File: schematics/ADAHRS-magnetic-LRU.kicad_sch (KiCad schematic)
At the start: 40 parts, among them Q1 2N2222, Q2 IRF7171M, Q3 Q2 - 2N2907, Q4 2N2222, Q5 IRF7171M, U1 OPA365-EP, U3 OPA365-EP

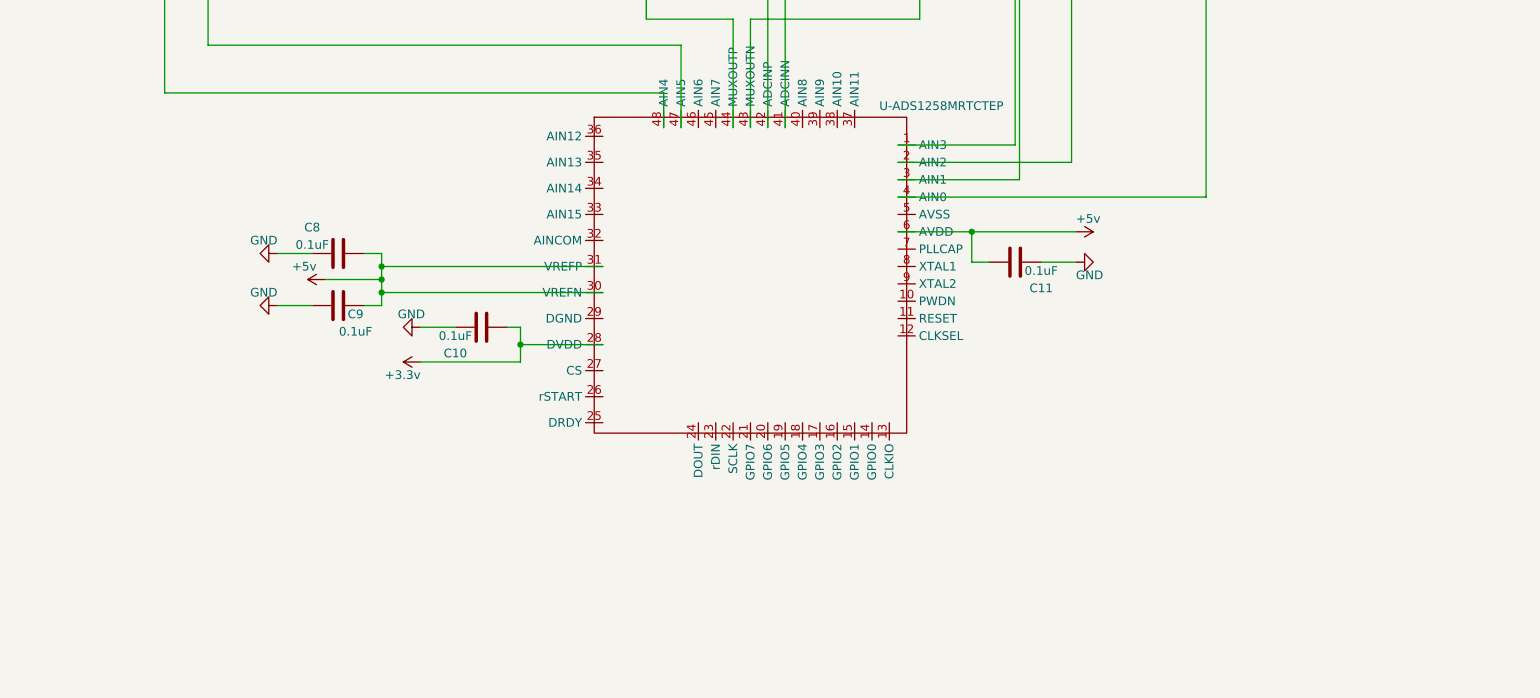
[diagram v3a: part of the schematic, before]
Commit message: Crystal oscillator and global var for MCU
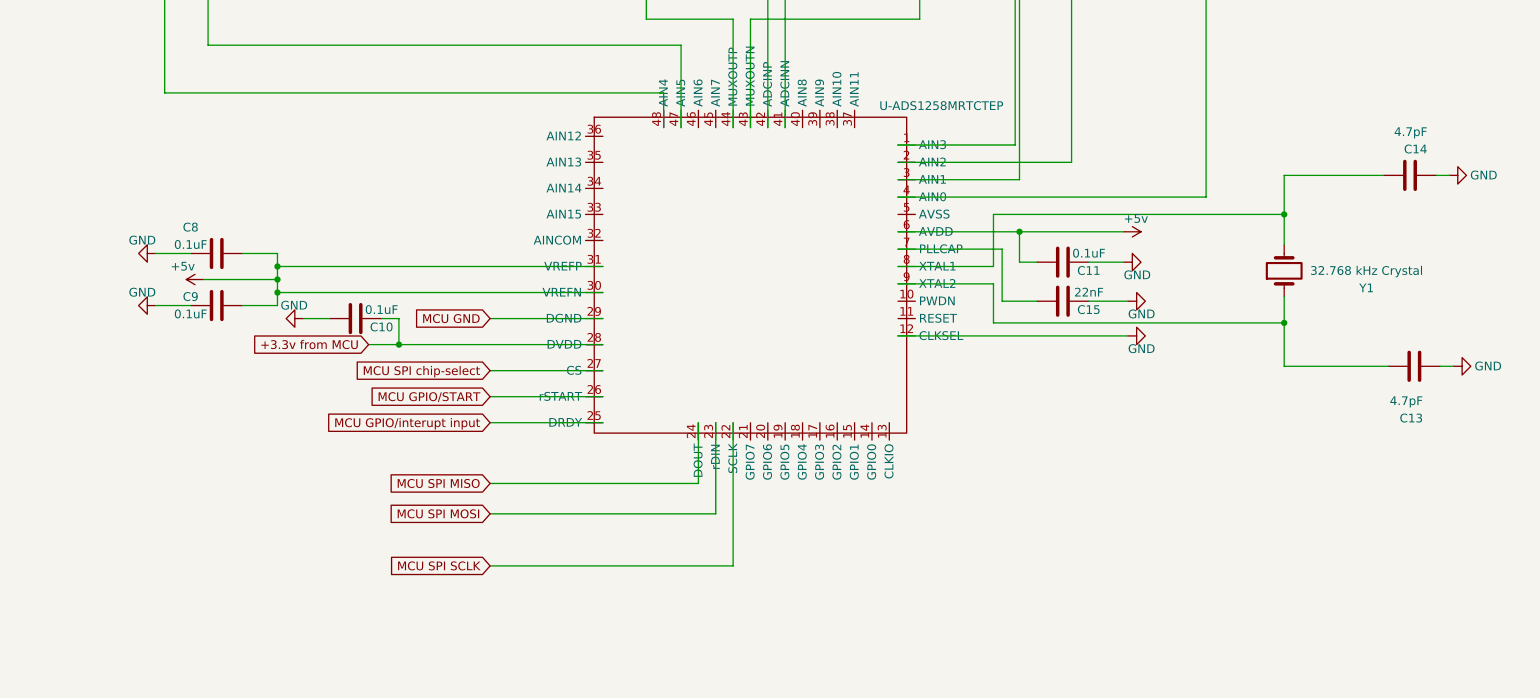
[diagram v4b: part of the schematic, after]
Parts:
- added C13, C14: 4.7pF, symbol Device:C
- added C15: 22nF, symbol Device:C
- added Y1: 32.768 kHz Crystal, symbol Device:Crystal
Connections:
- net +18v: now also U-ADS1258MRTCTEP.12 (CLKSEL), C13.1, C14.1, C15.1
- net MCU SPI SCLK: now reaches U-ADS1258MRTCTEP.22 (SCLK)
- net MCU SPI MOSI: now reaches U-ADS1258MRTCTEP.23 (rDIN)
- net MCU SPI MISO: now reaches U-ADS1258MRTCTEP.24 (DOUT)
- net MCU GPIO/interupt input: now reaches U-ADS1258MRTCTEP.25 (DRDY)
- net MCU GPIO/START: now reaches U-ADS1258MRTCTEP.26 (rSTART)
- net MCU SPI chip-select: now reaches U-ADS1258MRTCTEP.27 (CS)
- net MCU GND: now reaches U-ADS1258MRTCTEP.29 (DGND)
- net at U-ADS1258MRTCTEP.7 (PLLCAP): now also C15.2
- net at U-ADS1258MRTCTEP.8 (XTAL1): now also C14.2, Y1.2
- net at U-ADS1258MRTCTEP.9 (XTAL2): now also C13.2, Y1.1
- net +3.3v renamed +3.3v from MCU
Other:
- moved on the sheet: C10, C11, C8, C9

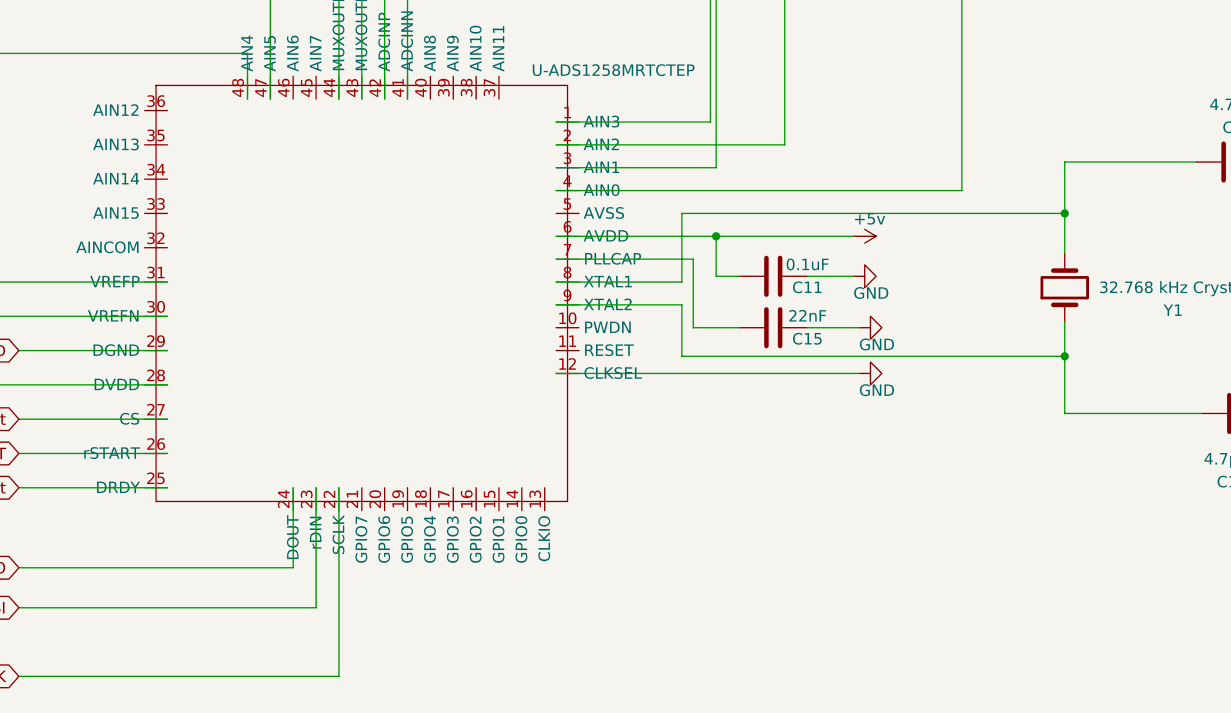
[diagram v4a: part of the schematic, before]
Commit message: revised capture v1_06
I will be adding filters the next versions for all. I wanted to connect every component and then add filters.
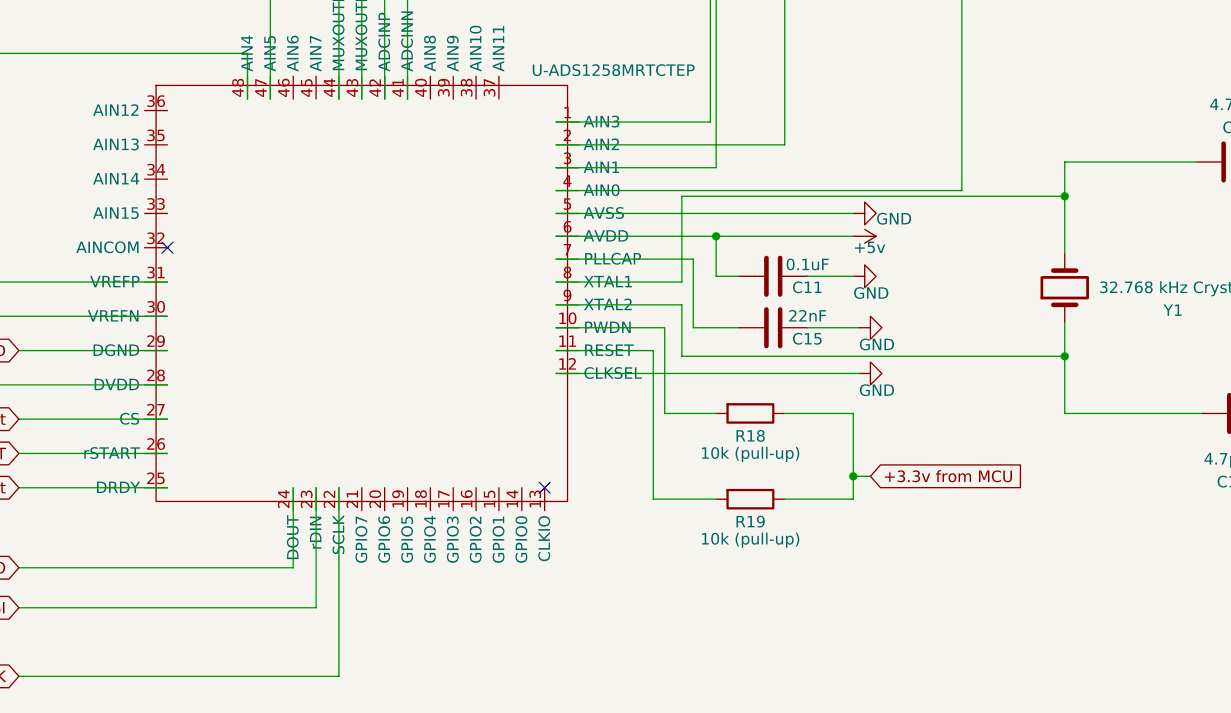
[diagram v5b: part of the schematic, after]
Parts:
- added R18, R19: 10k (pull-up), symbol Device:R
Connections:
- net +18v: now also U-ADS1258MRTCTEP.5 (AVSS)
- net +3.3v from MCU: now also R18.1, R19.1
- net at U-ADS1258MRTCTEP.10 (PWDN): now also R18.2
- net at U-ADS1258MRTCTEP.11 (RESET): now also R19.2
- no-connect marks 0 -> 2
